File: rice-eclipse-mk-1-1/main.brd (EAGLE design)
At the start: 100 x 80 mm, 53 parts, among them U1 LM1084ISX-5.0/NOPB, U2 THS4531IDRD8-M, U3 THS4531IDRD8-M, U4 THS4531IDRD8-M, U5 THS4531IDRD8-M, X1 2540-5

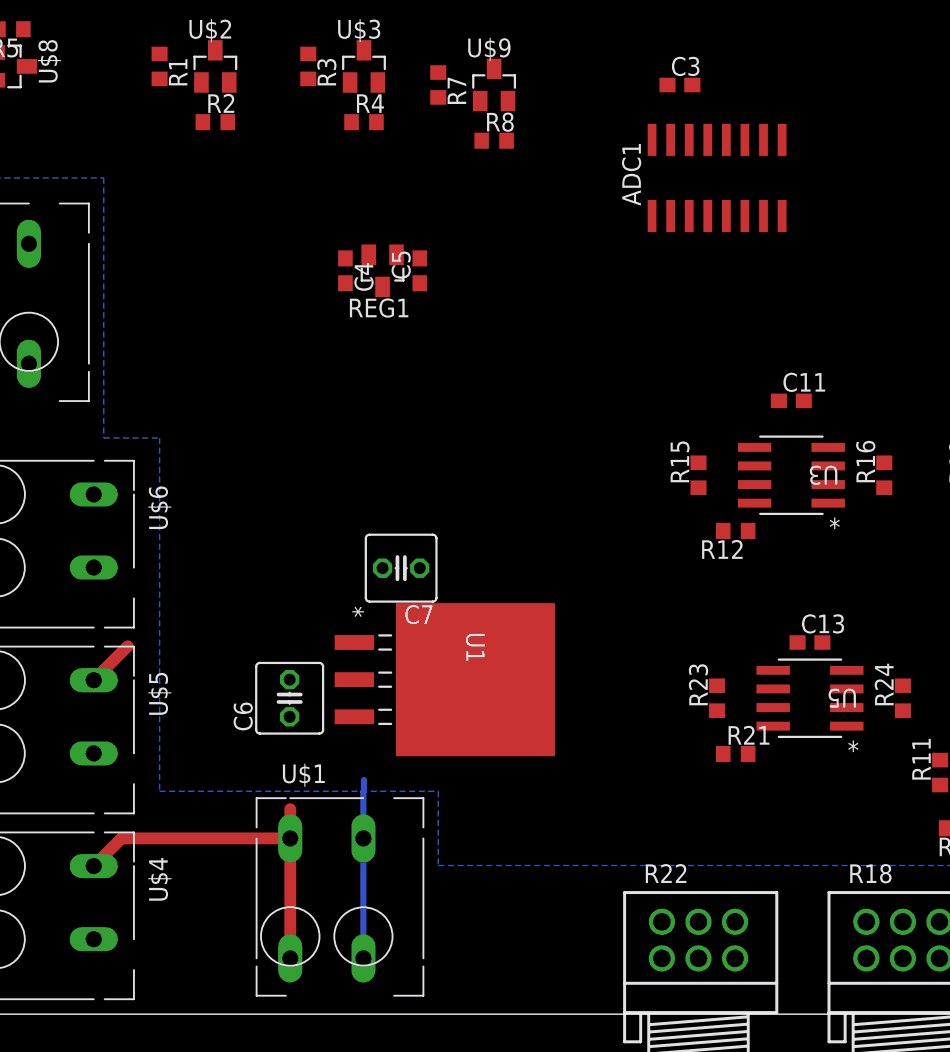
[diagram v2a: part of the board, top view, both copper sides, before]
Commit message: Added RPI GPIO connections.
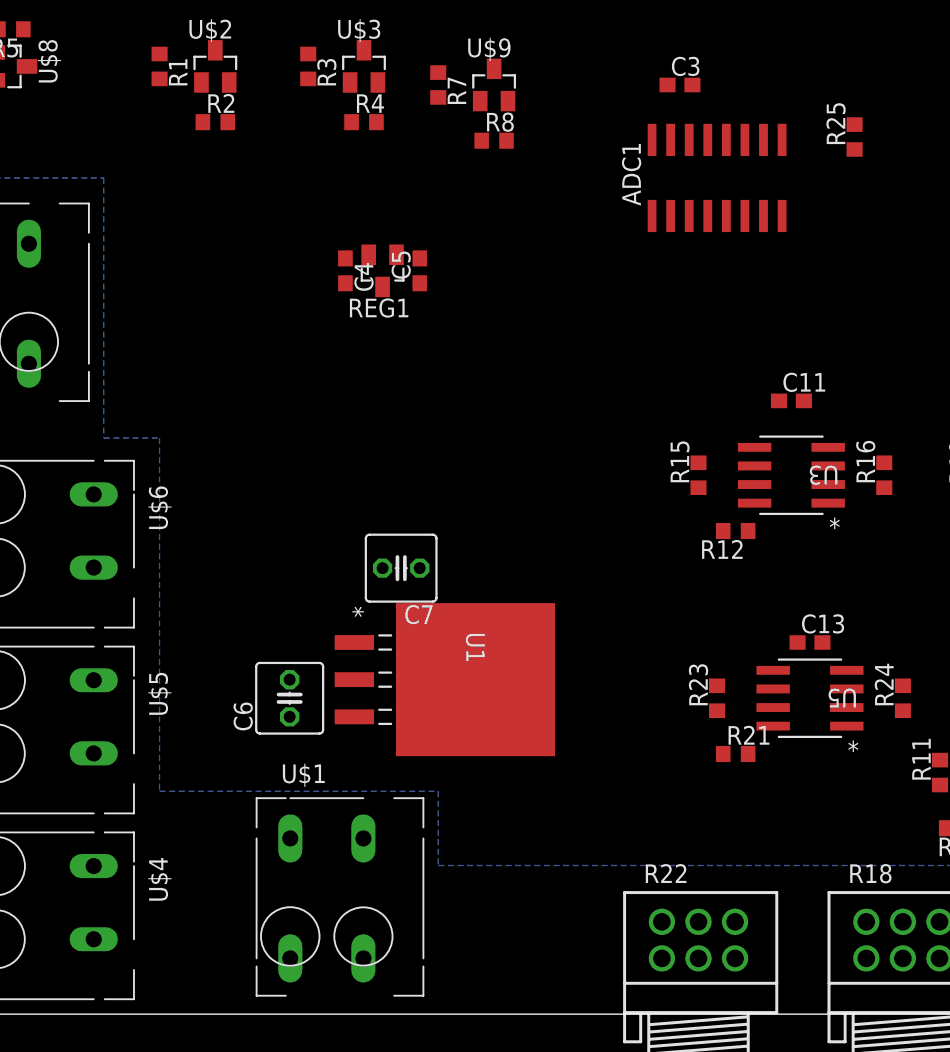
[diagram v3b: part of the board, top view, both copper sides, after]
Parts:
- added R25: 500K, rcl:R0603
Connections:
- net RPI_GPIO_19 renamed MOSI
- net RPI_GPIO_21 renamed MISO
- net RPI_GPIO_23 renamed SCLK
- net RPI_GPIO_24 renamed ADC2_CS
- net RPI_GPIO_26 renamed ADC3_CS
- removed net RPI_GPIO_11: X1.11
- removed net RPI_GPIO_13: X1.13
- removed net RPI_GPIO_15: X1.15
- removed net RPI_GPIO_16: X1.16
- removed net RPI_GPIO_2: X1.2
- removed net RPI_GPIO_22: X1.22
- removed net RPI_GPIO_6: X1.6
- new net ADC1_CS: R25.1, X1.22
- net +3V3: now also R25.2
- net +5V: now also X1.2
- net CTRL_SOLENOID_1: now also X1.11
- net CTRL_SOLENOID_2: now also X1.13
- net CTRL_SOLENOID_3: now also X1.15
- net GND: now also X1.6
- net IGNITION_RELAY: now also X1.16
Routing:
- net +12V: track 24.4 -> 0.00 mm
- net GND: track 12.2 -> 0.00 mm
- net +5V: track 3.29 -> 0.00 mm
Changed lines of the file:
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@@
 <attribute name="OC_NEWARK" value="unknown" x="99.06" y="58.42" size="1.778" layer="27" rot="R90" display="off"/>
 </element>
+<element name="R25" library="rcl" library_urn="urn:adsk.eagle:library:334" package="R0603" package3d_urn="urn:adsk.eagle:package:23555/2" value="500K" x="64.008" y="59.944" rot="R90"/>
 </elements>
 <signals>
@@
 <vertex x="0" y="71.12"/>
 </polygon>
-<wire x1="30.44" y1="3.81" x2="30.44" y2="12.01" width="0.4064" layer="16"/>
-<wire x1="30.44" y1="12.01" x2="30.44" y2="15.2" width="0.4064" layer="16"/>
-<wire x1="30.44" y1="15.2" x2="30.48" y2="15.24" width="0.4064" layer="16" curve="-90"/>
-<wire x1="30.48" y1="15.24" x2="30.48" y2="15.494" width="0.4064" layer="16"/>
-<wire x1="30.48" y1="15.494" x2="30.48" y2="16.002" width="0.4064" layer="16"/>
+<contactref element="X1" pad="6"/>
 <wire x1="74.9554" y1="37.465" x2="76.62" y2="40.64" width="0" layer="19" extent="1-1"/>
 <wire x1="60.54" y1="41.91" x2="74.9554" y2="37.465" width="0" layer="19" extent="1-1"/>
@@
 <wire x1="5.25" y1="63.82" x2="21.27" y2="63.67" width="0" layer="19" extent="1-1"/>
 <wire x1="2.54" y1="63.92" x2="5.25" y2="63.82" width="0" layer="19" extent="1-1"/>
+<wire x1="8.89" y1="77.47" x2="5.25" y2="63.82" width="0" layer="19" extent="1-1"/>
 <wire x1="31.75" y1="30.48" x2="29.21" y2="49.95" width="0" layer="19" extent="1-1"/>
-<wire x1="29.8196" y1="25.4" x2="25.4" y2="22.86" width="0" layer="19" extent="1-1"/>
+<wire x1="29.8196" y1="25.4" x2="31.75" y2="30.48" width="0" layer="19" extent="1-1"/>
+<wire x1="25.4" y1="22.86" x2="29.8196" y2="25.4" width="0" layer="19" extent="1-1"/>
+<wire x1="30.44" y1="12.01" x2="25.4" y2="22.86" width="0" layer="19" extent="1-1"/>
+<wire x1="30.44" y1="3.81" x2="30.44" y2="12.01" width="0" layer="19" extent="1-1"/>
 <wire x1="12.01" y1="17.82" x2="25.4" y2="22.86" width="0" layer="19" extent="1-1"/>
 <wire x1="3.81" y1="17.82" x2="12.01" y2="17.82" width="0" layer="19" extent="1-1"/>
@@
 <contactref element="U$4" pad="A1"/>
 <contactref element="U$4" pad="B1"/>
-<wire x1="25.44" y1="3.81" x2="25.44" y2="12.01" width="0.8128" layer="1"/>
-<wire x1="25.44" y1="12.01" x2="25.44" y2="14.01" width="0.8128" layer="1"/>
-<wire x1="25.44" y1="12.01" x2="13.9" y2="12.01" width="0.8128" layer="1"/>
-<wire x1="13.9" y1="12.01" x2="12.01" y2="10.12" width="0.8128" layer="1"/>
 <wire x1="31.75" y1="49.7" x2="34.29" y2="49.95" width="0" layer="19" extent="1-1"/>
 <wire x1="29.8196" y1="20.32" x2="31.75" y2="49.7" width="0" layer="19" extent="1-1"/>
 <wire x1="25.4" y1="20.32" x2="29.8196" y2="20.32" width="0" layer="19" extent="1-1"/>
-<wire x1="25.44" y1="14.01" x2="25.4" y2="20.32" width="0" layer="19" extent="1-1"/>
+<wire x1="25.44" y1="12.01" x2="25.4" y2="20.32" width="0" layer="19" extent="1-1"/>
+<wire x1="25.44" y1="3.81" x2="25.44" y2="12.01" width="0" layer="19" extent="1-1"/>
+<wire x1="12.01" y1="10.12" x2="25.44" y2="12.01" width="0" layer="19" extent="1-1"/>
 <wire x1="3.81" y1="10.12" x2="12.01" y2="10.12" width="0" layer="19" extent="1-1"/>
 </signal>
@@
 <contactref element="ADC1" pad="15"/>
 <contactref element="C3" pad="1"/>
-<wire x1="79.9846" y1="37.465" x2="78.32" y2="40.64" width="0" layer="19" extent="1-1"/>
-<wire x1="72.81" y1="33.02" x2="79.9846" y2="37.465" width="0" layer="19" extent="1-1"/>
-<wire x1="62.2046" y1="37.465" x2="72.81" y2="33.02" width="0" layer="19" extent="1-1"/>
-<wire x1="58.84" y1="41.91" x2="62.2046" y2="37.465" width="0" layer="19" extent="1-1"/>
+<contactref element="R25" pad="2"/>
+<wire x1="51.435" y1="59.75" x2="64.008" y2="60.794" width="0" layer="19" extent="1-1"/>
+<wire x1="50.165" y1="59.75" x2="51.435" y2="59.75" width="0" layer="19" extent="1-1"/>
+<wire x1="51.22" y1="63.5" x2="51.435" y2="59.75" width="0" layer="19" extent="1-1"/>
+<wire x1="58.84" y1="41.91" x2="51.435" y2="59.75" width="0" layer="19" extent="1-1"/>
+<wire x1="62.2046" y1="37.465" x2="58.84" y2="41.91" width="0" layer="19" extent="1-1"/>
 <wire x1="55.03" y1="33.02" x2="62.2046" y2="37.465" width="0" layer="19" extent="1-1"/>
 <wire x1="60.11" y1="25.4" x2="55.03" y2="33.02" width="0" layer="19" extent="1-1"/>
 <wire x1="63.4746" y1="22.225" x2="60.11" y2="25.4" width="0" layer="19" extent="1-1"/>
 <wire x1="56.73" y1="17.78" x2="63.4746" y2="22.225" width="0" layer="19" extent="1-1"/>
+<wire x1="72.81" y1="33.02" x2="62.2046" y2="37.465" width="0" layer="19" extent="1-1"/>
+<wire x1="79.9846" y1="37.465" x2="72.81" y2="33.02" width="0" layer="19" extent="1-1"/>
+<wire x1="78.32" y1="40.64" x2="79.9846" y2="37.465" width="0" layer="19" extent="1-1"/>
 <wire x1="70.27" y1="12.7" x2="63.4746" y2="22.225" width="0" layer="19" extent="1-1"/>
 <wire x1="77.4446" y1="17.145" x2="70.27" y2="12.7" width="0" layer="19" extent="1-1"/>
 <wire x1="75.78" y1="20.32" x2="77.4446" y2="17.145" width="0" layer="19" extent="1-1"/>
-<wire x1="51.435" y1="59.75" x2="58.84" y2="41.91" width="0" layer="19" extent="1-1"/>
-<wire x1="50.165" y1="59.75" x2="51.435" y2="59.75" width="0" layer="19" extent="1-1"/>
-<wire x1="51.22" y1="63.5" x2="51.435" y2="59.75" width="0" layer="19" extent="1-1"/>
 <wire x1="30.8" y1="51.9" x2="50.165" y2="59.75" width="0" layer="19" extent="1-1"/>
 <wire x1="29.21" y1="51.65" x2="30.8" y2="51.9" width="0" layer="19" extent="1-1"/>
@@
 <contactref element="U$5" pad="B1"/>
 <contactref element="U1" pad="4"/>
-<wire x1="14.336" y1="25.146" x2="12.01" y2="22.82" width="0.8128" layer="1"/>
-<wire x1="38.1" y1="22.86" x2="34.29" y2="30.48" width="0" layer="19" extent="1-1"/>
-<wire x1="29.8196" y1="22.86" x2="38.1" y2="22.86" width="0" layer="19" extent="1-1"/>
-<wire x1="14.336" y1="25.146" x2="29.8196" y2="22.86" width="0" layer="19" extent="1-1"/>
-<wire x1="3.81" y1="22.82" x2="12.01" y2="22.82" width="0" layer="19" extent="1-1"/>
+<contactref element="X1" pad="2"/>
+<wire x1="3.81" y1="22.82" x2="3.81" y2="77.47" width="0" layer="19" extent="1-1"/>
+<wire x1="12.01" y1="22.82" x2="3.81" y2="22.82" width="0" layer="19" extent="1-1"/>
+<wire x1="29.8196" y1="22.86" x2="12.01" y2="22.82" width="0" layer="19" extent="1-1"/>
+<wire x1="38.1" y1="22.86" x2="29.8196" y2="22.86" width="0" layer="19" extent="1-1"/>
+<wire x1="34.29" y1="30.48" x2="38.1" y2="22.86" width="0" layer="19" extent="1-1"/>
 </signal>
 <signal name="N$13">
@@
 <signal name="CTRL_SOLENOID_1">
 <contactref element="R3" pad="1"/>
+<contactref element="X1" pad="11"/>
+<wire x1="16.51" y1="74.93" x2="26.67" y2="65.62" width="0" layer="19" extent="1-1"/>
 </signal>
 <signal name="SOLENOID_1_NEGATIVE">
@@
 <signal name="CTRL_SOLENOID_2">
 <contactref element="R5" pad="1"/>
+<contactref element="X1" pad="13"/>
+<wire x1="7.2" y1="67.31" x2="19.05" y2="74.93" width="0" layer="19" extent="1-1"/>
 </signal>
 <signal name="SOLENOID_2_NEGATIVE">
@@
 <signal name="CTRL_SOLENOID_3">
 <contactref element="R7" pad="1"/>
+<contactref element="X1" pad="15"/>
+<wire x1="21.59" y1="74.93" x2="35.56" y2="64.35" width="0" layer="19" extent="1-1"/>
 </signal>
 <signal name="SOLENOID_3_NEGATIVE">
@@
 <signal name="IGNITION_RELAY">
 <contactref element="R1" pad="1"/>
+<contactref element="X1" pad="16"/>
+<wire x1="16.51" y1="65.62" x2="21.59" y2="77.47" width="0" layer="19" extent="1-1"/>
 </signal>
 <signal name="RELAY_NEGATIVE">
@@
 <contactref element="X1" pad="1"/>
 </signal>
-<signal name="RPI_GPIO_2">
-<contactref element="X1" pad="2"/>
-</signal>
 <signal name="RPI_GPIO_3">
 <contactref element="X1" pad="3"/>
@@
 <contactref element="X1" pad="5"/>
 </signal>
-<signal name="RPI_GPIO_6">
-<contactref element="X1" pad="6"/>
-</signal>
 <signal name="RPI_GPIO_7">
 <contactref element="X1" pad="7"/>
 </signal>
-<signal name="RPI_GPIO_8">
-<contactref element="X1" pad="8"/>
-</signal>
 <signal name="RPI_GPIO_40">
 <contactref element="X1" pad="40"/>
@@
 <contactref element="X1" pad="27"/>
 </signal>
-<signal name="RPI_GPIO_26">
+<signal name="ADC3_CS">
 <contactref element="X1" pad="26"/>
 </signal>
@@
 <contactref element="X1" pad="25"/>
 </signal>
-<signal name="RPI_GPIO_24">
-<contactref element="X1" pad="24"/>
-</signal>
-<signal name="RPI_GPIO_23">
+<signal name="SCLK">
 <contactref element="X1" pad="23"/>
 </signal>
-<signal name="RPI_GPIO_22">
+<signal name="ADC1_CS">
 <contactref element="X1" pad="22"/>
-</signal>
-<signal name="RPI_GPIO_21">
+<contactref element="R25" pad="1"/>
+<wire x1="29.21" y1="77.47" x2="64.008" y2="59.094" width="0" layer="19" extent="1-1"/>
+</signal>
+<signal name="MISO">
 <contactref element="X1" pad="21"/>
 </signal>
@@
 <contactref element="X1" pad="20"/>
 </signal>
-<signal name="RPI_GPIO_19">
+<signal name="MOSI">
 <contactref element="X1" pad="19"/>
 </signal>
@@
 <contactref element="X1" pad="17"/>
 </signal>
-<signal name="RPI_GPIO_16">
-<contactref element="X1" pad="16"/>
-</signal>
-<signal name="RPI_GPIO_15">
-<contactref element="X1" pad="15"/>
-</signal>
 <signal name="RPI_GPIO_14">
 <contactref element="X1" pad="14"/>
@@
 <signal name="RPI_GPIO_12">
 <contactref element="X1" pad="12"/>
-</signal>
-<signal name="RPI_GPIO_13">
-<contactref element="X1" pad="13"/>
-</signal>
-<signal name="RPI_GPIO_11">
-<contactref element="X1" pad="11"/>
 </signal>
 <signal name="RPI_GPIO_10">
@@
 <wire x1="91.36" y1="71.97" x2="96.36" y2="71.97" width="0" layer="19" extent="1-1"/>
 </signal>
+<signal name="RPI_GPIO_8">
+<contactref element="X1" pad="8"/>
+</signal>
+<signal name="ADC2_CS">
+<contactref element="X1" pad="24"/>
+</signal>
 </signals>

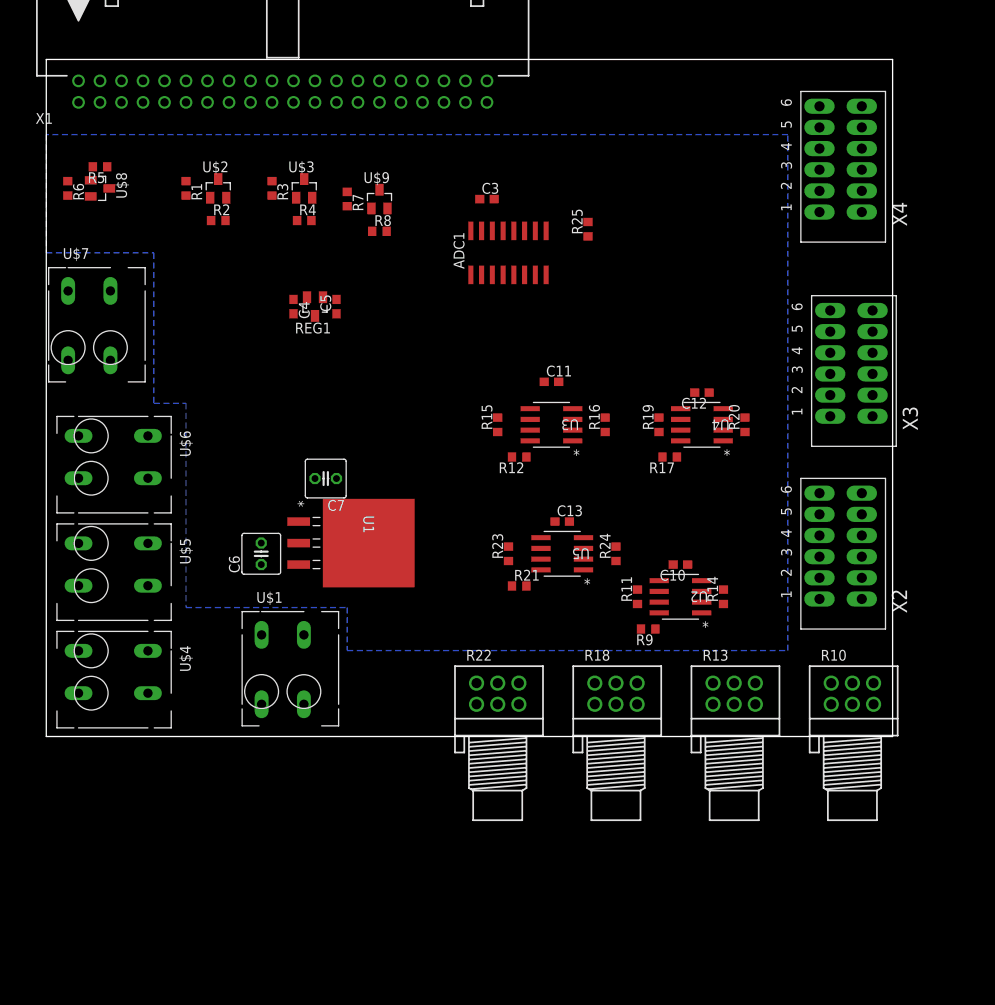
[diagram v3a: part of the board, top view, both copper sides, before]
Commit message: EAGLE stuff
- changed 6 pin connectors to 4 pin for loadcells 1-4
- deleted load cell 5 connector
- added debugging slide switches
- board rearranged
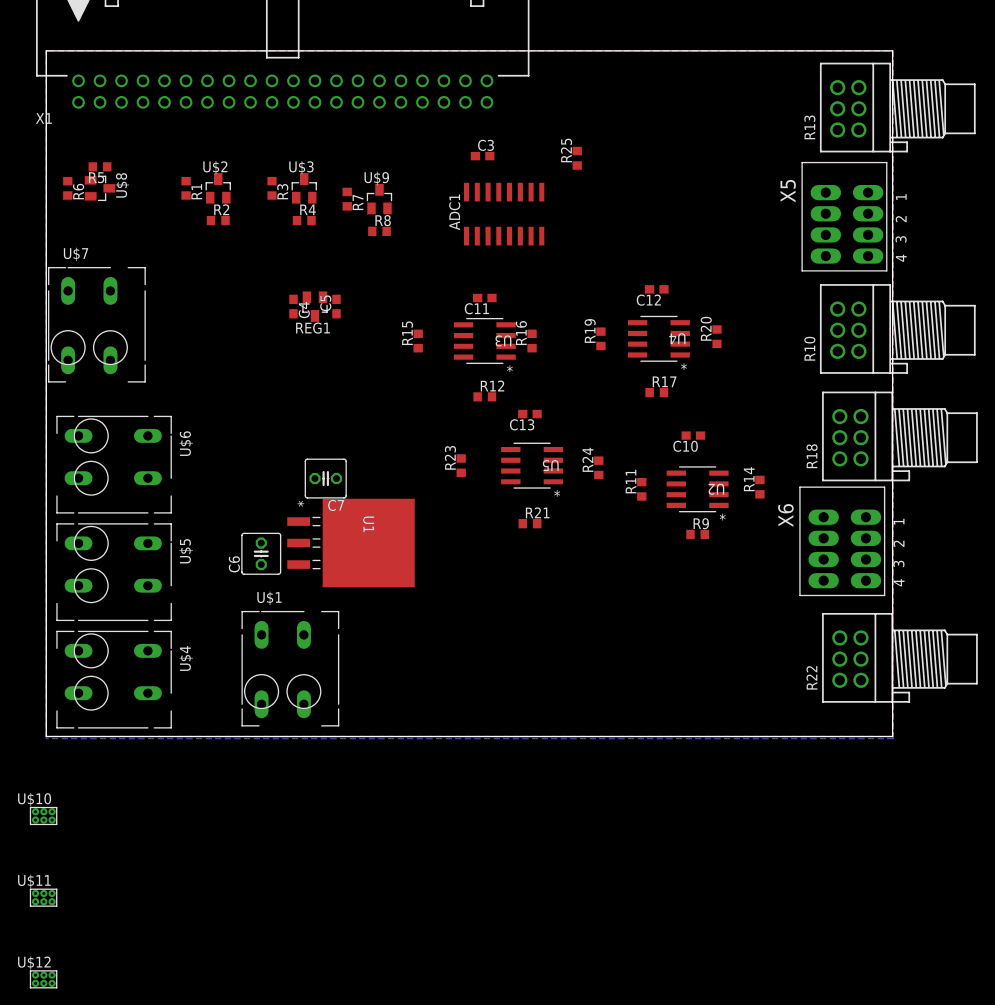
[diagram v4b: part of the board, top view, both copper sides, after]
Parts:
- removed X2, X3, X4: (no value), con-phoenix-250-extra:1770924
- added U$10, U$11, U$12: SLIDE_SW, SLIDE_SW:SLIDE_SW
- added X5, X6: (no value), con-phoenix-250-extra:1770908
- moved R13 71.9 mm to (96.0, 74.2), turned to 90 degrees
- moved R10 44.2 mm to (96.0, 48.0), turned to 90 degrees
- moved R22 43.3 mm to (96.3, 9.14), turned to 90 degrees
- moved R18 42.8 mm to (96.3, 35.3), turned to 90 degrees
- moved C10 15.3 mm to (76.5, 35.6)
- moved R15 13.7 mm to (43.9, 46.7)
- moved R14 13.7 mm to (84.3, 29.5)
- moved C12 13.3 mm to (72.1, 52.8)
- moved C13 13.3 mm to (57.1, 38.1), turned to 180 degrees
- moved R16 13.1 mm to (57.4, 46.7)
- moved U2 12.9 mm to (77.0, 29.2)
- moved R11 12.7 mm to (70.4, 29.2)
- moved C11 12.7 mm to (51.8, 51.8), turned to 180 degrees
- moved U3 12.7 mm to (51.8, 46.7)
- moved R9 12.6 mm to (77.0, 23.9), turned to 0 degrees
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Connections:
- removed net LC_5_OUT+: X3.P$3, X3.P$9
- removed net LC_5_OUT-: X3.P$10, X3.P$4
- removed net N$10: X4.P$10, X4.P$4
- removed net N$11: X4.P$11, X4.P$5
- removed net N$12: X4.P$12, X4.P$6
- removed net N$9: X4.P$3, X4.P$9
- removed net PT_OUT+: X3.P$11, X3.P$5
- removed net PT_OUT-: X3.P$12, X3.P$6
- removed net TC_1_OUT: X4.P$1, X4.P$7
- removed net TC_2_OUT: X4.P$2, X4.P$8
- new net DEBUG_3V3: U$11.P$1
- new net DEBUG_5V: U$12.P$3
- net +12V: now also U$10.P$2, U$10.P$3
- net +3V3: now also U$11.P$3
- net +5V: now also U$12.P$2
- net LC_1_OUT+: now also X5.P$1, X5.P$5; no longer X2.P$1, X2.P$7
- net LC_1_OUT-: now also X5.P$2, X5.P$6; no longer X2.P$2, X2.P$8
- net LC_2_OUT+: now also X5.P$3, X5.P$7; no longer X2.P$3, X2.P$9
- net LC_2_OUT-: now also X5.P$4, X5.P$8; no longer X2.P$10, X2.P$4
- net LC_3_OUT+: now also X6.P$1, X6.P$5; no longer X2.P$11, X2.P$5
- net LC_3_OUT-: now also X6.P$2, X6.P$6; no longer X2.P$12, X2.P$6
- net LC_4_OUT+: now also X6.P$3, X6.P$7; no longer X3.P$1, X3.P$7
- net LC_4_OUT-: now also X6.P$4, X6.P$8; no longer X3.P$2, X3.P$8
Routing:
- added copper zone on layer 1, net GND
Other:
- board size 100 x 80 mm -> 100 x 81 mm
